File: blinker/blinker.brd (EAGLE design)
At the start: 54.3 x 47 mm, 12 parts, among them IC1 LM555N

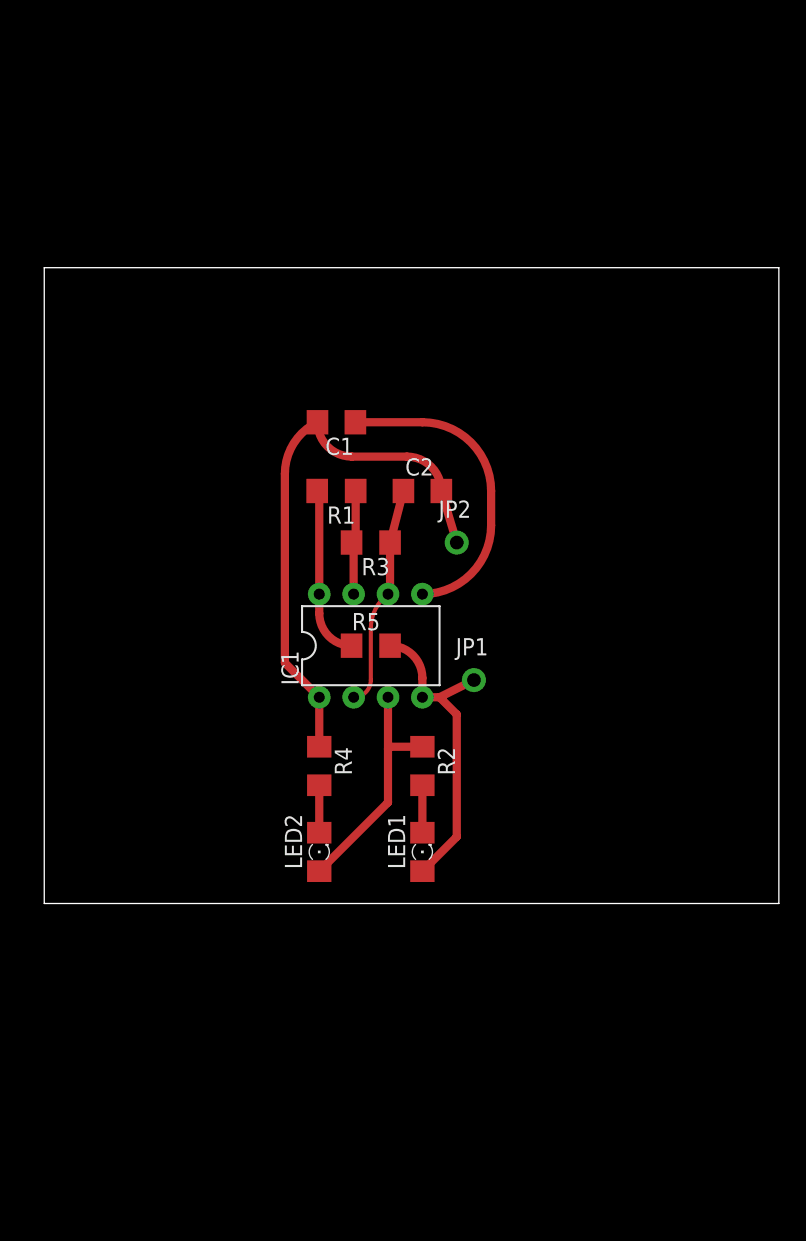
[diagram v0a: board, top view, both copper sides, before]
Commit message: Blinker component size changes
Also added gitignore, and some datasheets
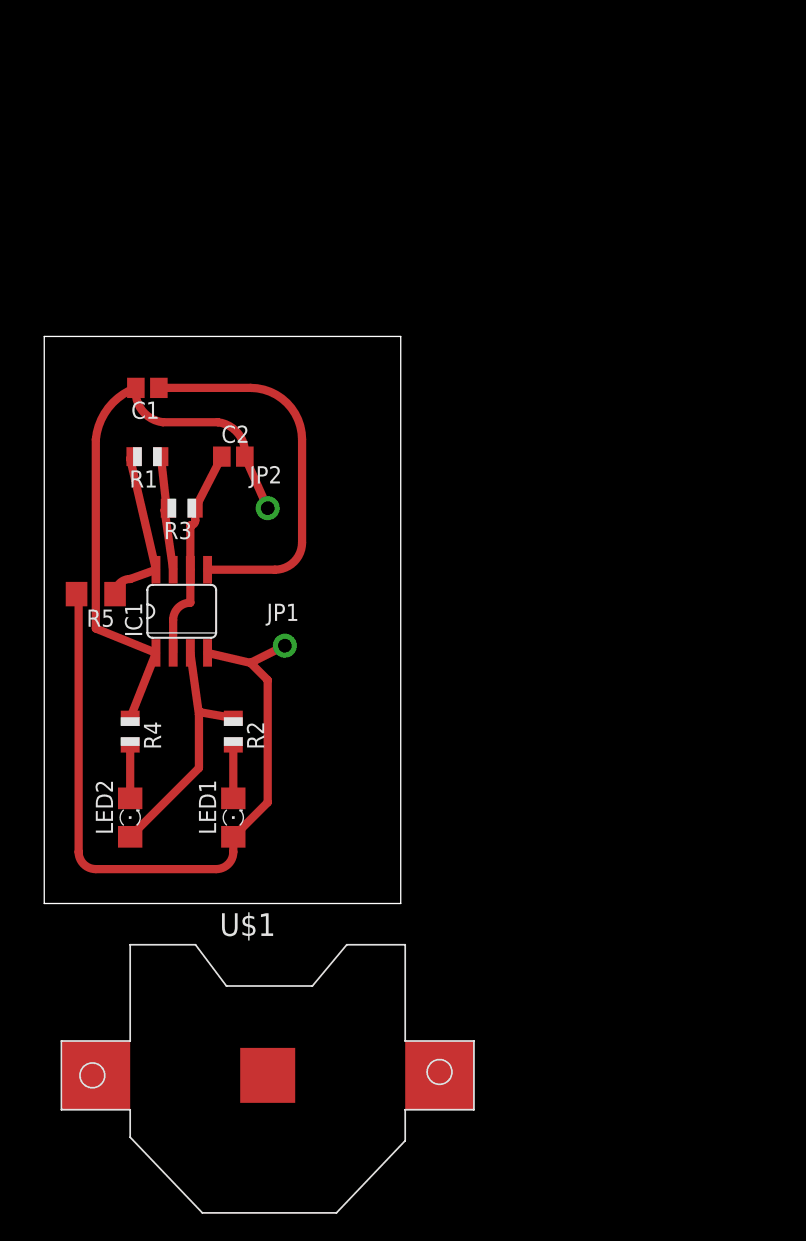
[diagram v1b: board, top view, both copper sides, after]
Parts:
- added U$1: (no value), adafruit:CR2032-SMD
- C1, C2: device adafruit:C1206 -> adafruit:C0805
- IC1: value LM555N -> LM555D; device adafruit:DIL08-ROUND -> adafruit:SO08
- R1, R2, R3, R4: device adafruit:R1206 -> adafruit:R0805
- moved R5 20.7 mm to (3.81, 22.9), turned to 180 degrees
- moved C2 14.2 mm to (14.0, 33.0)
- moved R1 14.2 mm to (7.62, 33.0)
- moved LED1 14.2 mm to (14.0, 6.35)
- moved LED2 14.2 mm to (6.35, 6.35)
- moved R2 14.2 mm to (14.0, 12.7)
- moved R4 14.2 mm to (6.35, 12.7)
- moved C1 14.2 mm to (7.62, 38.1)
- moved IC1 14.2 mm to (10.2, 21.6)
- moved JP1 14.2 mm to (17.8, 19.1)
- moved JP2 14.2 mm to (16.5, 29.2)
- moved R3 14.2 mm to (10.2, 29.2)
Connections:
- net GND: now also U$1.-
- net V+: now also U$1.+$1
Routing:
- net V+: track 35.8 -> 65.7 mm
- net N$5: track 21.9 -> 27.6 mm
- net GND: track 41.0 -> 43.5 mm
- net N$2: track 17.6 -> 18.4 mm
- net N$4: track 7.99 -> 8.70 mm
- net CONN: track 16.3 -> 15.7 mm
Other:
- board size 54.3 x 47 mm -> 26.3 x 41.9 mm

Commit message: PCB design is ready for Blinker
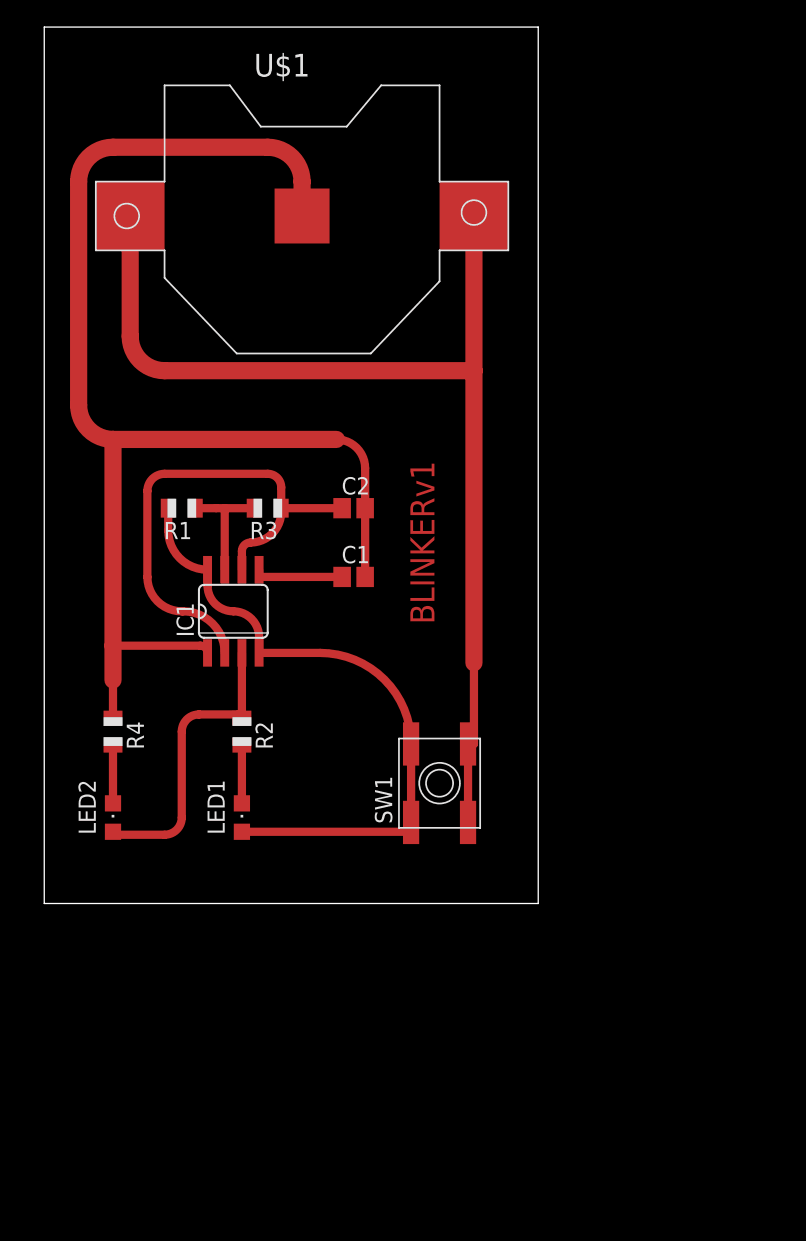
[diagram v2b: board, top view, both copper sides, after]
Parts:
- removed JP1, JP2: (no value), adafruit:1X01-CLEANBIG
- removed R5: 0R, adafruit:R1206
- added SW1: SPST_TACT5.2VARIANT, mokerek:5.2X5.2
- LED1, LED2: value green -> red; device adafruit:1206 -> adafruit:CHIPLED_0805
- U$1: value (none) -> CR2032
- moved U$1 63.6 mm to (19.1, 50.8)
- moved C1 20.7 mm to (22.9, 24.1), turned to 0 degrees
- moved C2 9.67 mm to (22.9, 29.2)
- moved R3 6.35 mm to (16.5, 29.2)
- moved R1 4.58 mm to (10.2, 29.2)
- moved IC1 3.81 mm to (14.0, 21.6)
- moved LED2 1.27 mm to (5.08, 6.35), turned to 0 degrees
- moved R4 1.27 mm to (5.08, 12.7)
- moved LED1 0.63 mm to (14.6, 6.35), turned to 0 degrees
- moved R2 0.63 mm to (14.6, 12.7)
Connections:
- new net N$6: SW1.A, SW1.A', U$1.+$1, U$1.+$2
- net GND: no longer JP2.1
- net V+: now also SW1.B, SW1.B'; no longer JP1.1, R5.1, R5.2, U$1.+$1
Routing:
- net N$6: track 0.00 -> 80.6 mm
- net GND: track 43.5 -> 96.6 mm
- net CONN: track 15.7 -> 37.0 mm
- net N$5: track 27.6 -> 6.67 mm
- net V+: track 65.7 -> 47.5 mm
- net N$2: track 18.4 -> 21.9 mm
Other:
- board size 26.3 x 41.9 mm -> 36.5 x 64.8 mm
- board text added: "BLINKERv1"

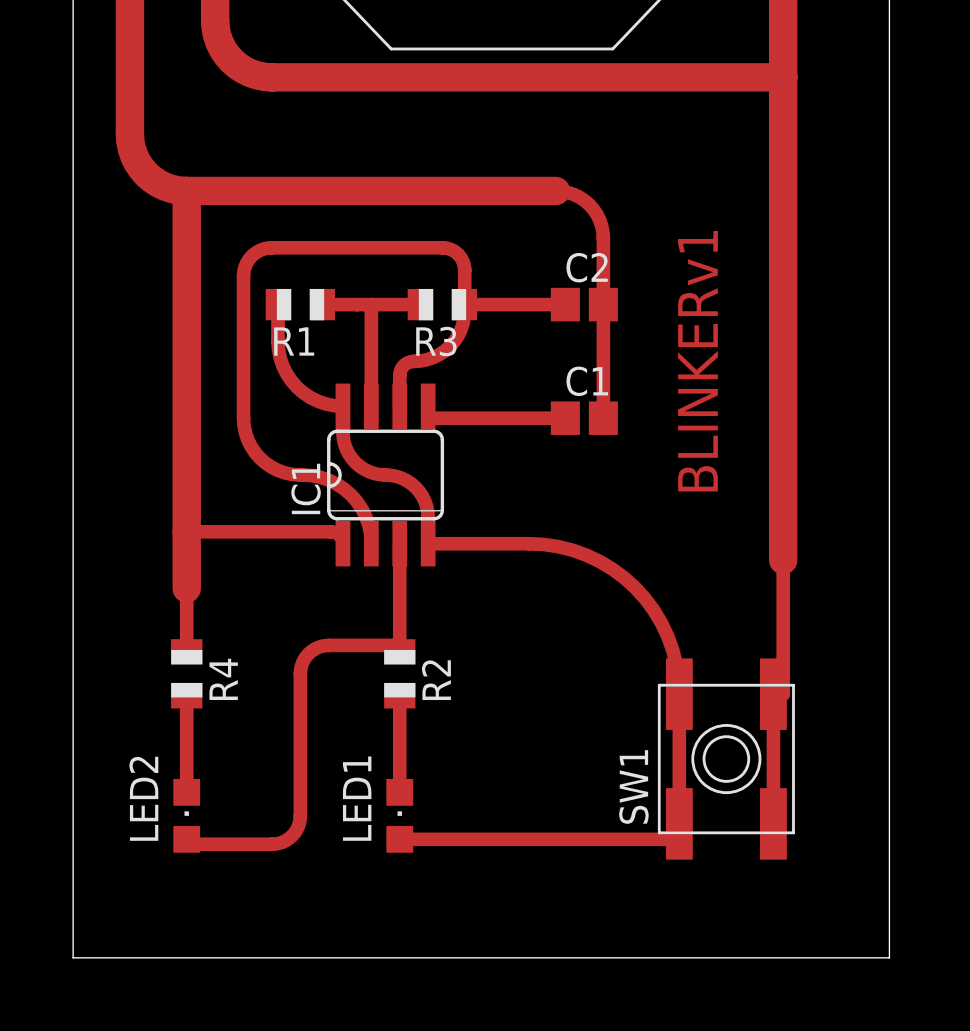
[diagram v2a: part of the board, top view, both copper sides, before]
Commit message: Added ground plane
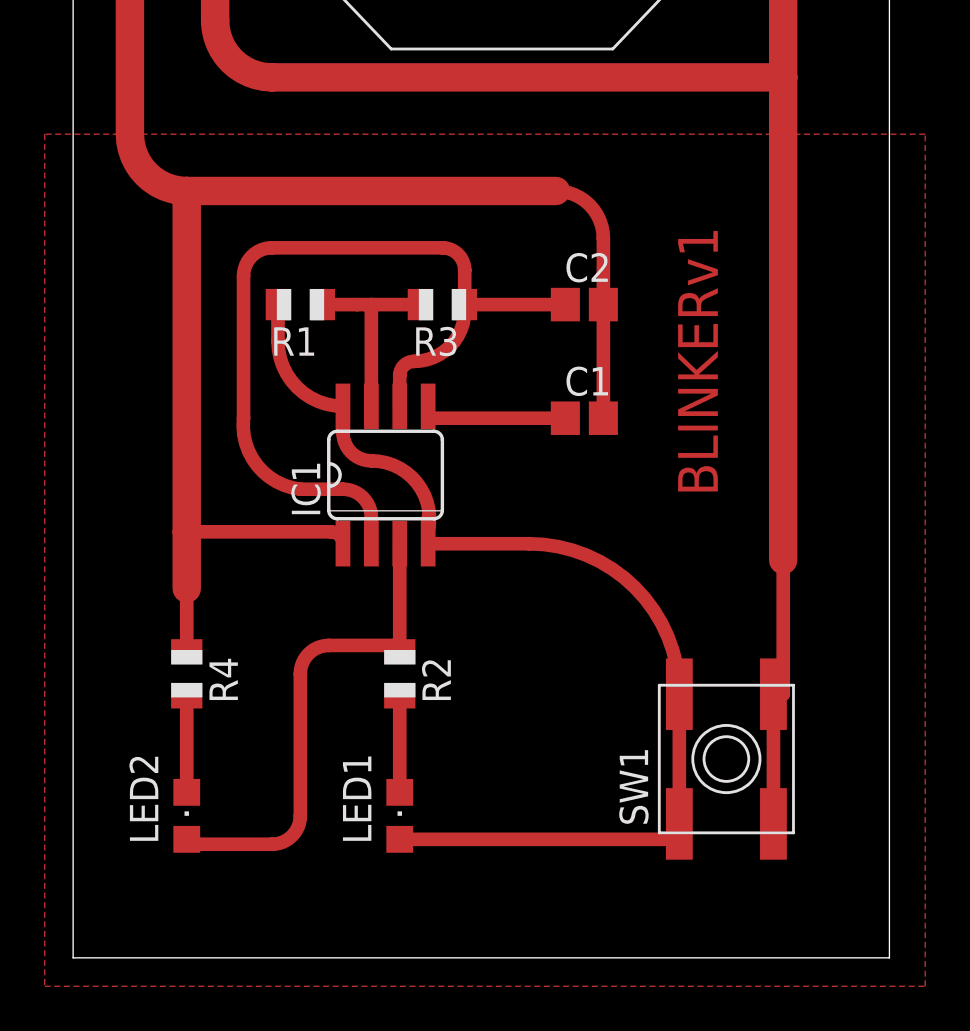
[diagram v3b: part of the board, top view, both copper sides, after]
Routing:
- net CONN: track 37.0 -> 37.9 mm
- added copper zone on layer 1, net GND
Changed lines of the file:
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@@
 </class>
 </classes>
-<designrules name="default">
+<designrules name="default *">
 <description language="de">&lt;b&gt;EAGLE Design Rules&lt;/b&gt;
 &lt;p&gt;
@@
 <param name="mtCopper" value="0.035mm 0.035mm 0.035mm 0.035mm 0.035mm 0.035mm 0.035mm 0.035mm 0.035mm 0.035mm 0.035mm 0.035mm 0.035mm 0.035mm 0.035mm 0.035mm"/>
 <param name="mtIsolate" value="1.5mm 0.15mm 0.2mm 0.15mm 0.2mm 0.15mm 0.2mm 0.15mm 0.2mm 0.15mm 0.2mm 0.15mm 0.2mm 0.15mm 0.2mm"/>
-<param name="mdWireWire" value="8mil"/>
-<param name="mdWirePad" value="8mil"/>
-<param name="mdWireVia" value="8mil"/>
-<param name="mdPadPad" value="8mil"/>
-<param name="mdPadVia" value="8mil"/>
-<param name="mdViaVia" value="8mil"/>
-<param name="mdSmdPad" value="8mil"/>
-<param name="mdSmdVia" value="8mil"/>
-<param name="mdSmdSmd" value="8mil"/>
+<param name="mdWireWire" value="20mil"/>
+<param name="mdWirePad" value="20mil"/>
+<param name="mdWireVia" value="20mil"/>
+<param name="mdPadPad" value="20mil"/>
+<param name="mdPadVia" value="20mil"/>
+<param name="mdViaVia" value="20mil"/>
+<param name="mdSmdPad" value="20mil"/>
+<param name="mdSmdVia" value="20mil"/>
+<param name="mdSmdSmd" value="20mil"/>
 <param name="mdViaViaSameLayer" value="8mil"/>
 <param name="mnLayersViaInSmd" value="2"/>
@@
 <wire x1="2.54" y1="53.34" x2="2.54" y2="36.83" width="1.27" layer="1"/>
 <wire x1="2.54" y1="36.83" x2="5.08" y2="34.29" width="1.27" layer="1" curve="90"/>
+<polygon width="0.4064" layer="1">
+<vertex x="-1.27" y="36.83"/>
+<vertex x="-1.27" y="-1.27"/>
+<vertex x="38.1" y="-1.27"/>
+<vertex x="38.1" y="36.83"/>
+</polygon>
 </signal>
 <signal name="CONN">
@@
 <wire x1="8.89" y1="31.75" x2="7.62" y2="30.48" width="0.6096" layer="1" curve="90"/>
 <wire x1="7.62" y1="30.48" x2="7.62" y2="24.13" width="0.6096" layer="1"/>
-<wire x1="7.62" y1="24.13" x2="10.16" y2="21.59" width="0.6096" layer="1" curve="90"/>
-<wire x1="10.16" y1="21.59" x2="10.2616" y2="21.59" width="0.6096" layer="1"/>
-<wire x1="10.2616" y1="21.59" x2="13.335" y2="18.5166" width="0.6096" layer="1" curve="-90"/>
+<wire x1="7.62" y1="24.13" x2="10.16" y2="20.955" width="0.6096" layer="1" curve="90"/>
+<wire x1="10.16" y1="20.955" x2="12.065" y2="20.955" width="0.6096" layer="1"/>
+<wire x1="12.065" y1="20.955" x2="13.335" y2="19.685" width="0.6096" layer="1" curve="-90"/>
+<wire x1="13.335" y1="19.685" x2="13.335" y2="18.5166" width="0.6096" layer="1"/>
 </signal>
 <signal name="V+">
@@
 <wire x1="9.16" y1="27.5684" x2="12.065" y2="24.6634" width="0.6096" layer="1" curve="90"/>
 <wire x1="12.065" y1="24.6634" x2="12.065" y2="23.495" width="0.6096" layer="1"/>
-<wire x1="12.065" y1="23.495" x2="13.97" y2="21.59" width="0.6096" layer="1" curve="90"/>
-<wire x1="13.97" y1="21.59" x2="15.875" y2="19.685" width="0.6096" layer="1" curve="-90"/>
-<wire x1="15.875" y1="19.685" x2="15.875" y2="18.5166" width="0.6096" layer="1"/>
+<wire x1="15.875" y1="19.685" x2="15.875" y2="19.05" width="0.6096" layer="1"/>
+<wire x1="15.875" y1="19.05" x2="15.875" y2="18.5166" width="0.6096" layer="1"/>
 <wire x1="20.3794" y1="18.5166" x2="27.106" y2="11.79" width="0.6096" layer="1" curve="-90"/>
 <wire x1="27.106" y1="11.79" x2="27.106" y2="5.99" width="0.6096" layer="1"/>
@@
 <wire x1="14.605" y1="5.3" x2="27.106" y2="5.3" width="0.6096" layer="1"/>
 <wire x1="27.106" y1="5.3" x2="27.106" y2="5.99" width="0.6096" layer="1"/>
+<wire x1="12.065" y1="23.495" x2="13.335" y2="22.225" width="0.6096" layer="1" curve="90"/>
+<wire x1="13.335" y1="22.225" x2="15.875" y2="19.05" width="0.6096" layer="1" curve="-102.680383"/>
 </signal>
 <signal name="N$5">
